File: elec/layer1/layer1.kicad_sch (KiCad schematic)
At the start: 114 parts, among them U1 DEV-15583, U2 CD74HC4067SM, U3 CD74HC4067SM

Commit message: fix: layer1 pcb
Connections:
- net +3V3: no longer U1.3.3V_1, U1.3.3V_2
- no-connect marks 25 -> 28
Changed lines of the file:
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@@
 	)
 	(no_connect
+		(at 154.94 109.22)
+	)
+	(no_connect
 		(at 196.85 203.2)
 	)
@@
 	)
 	(no_connect
+		(at 232.41 193.04)
+	)
+	(no_connect
 		(at 102.87 217.17)
 	)
@@
 	)
 	(no_connect
+		(at 196.85 228.6)
+	)
+	(no_connect
 		(at 196.85 205.74)
 	)
@@
 	)
 	(symbol
-		(lib_id "power:+3V3")
-		(at 196.85 228.6 90)
-		(unit 1)
-		(exclude_from_sim no)
-		(in_bom yes)
-		(on_board yes)
-		(dnp no)
-		(fields_autoplaced yes)
-		(property "Reference" "#PWR049"
-			(at 200.66 228.6 0)
-			(effects
-				(font
-					(size 1.27 1.27)
-				)
-				(hide yes)
-			)
-		)
-		(property "Value" "+3V3"
-			(at 193.04 228.5999 90)
-			(effects
-				(font
-					(size 1.27 1.27)
-				)
-				(justify left)
-			)
-		)
-		(property "Footprint" ""
-			(at 196.85 228.6 0)
-			(effects
-				(font
-					(size 1.27 1.27)
-				)
-				(hide yes)
-			)
-		)
-		(property "Datasheet" ""
-			(at 196.85 228.6 0)
-			(effects
-				(font
-					(size 1.27 1.27)
-				)
-				(hide yes)
-			)
-		)
-		(property "Description" "Power symbol creates a global label with name \"+3V3\""
-			(at 196.85 228.6 0)
-			(effects
-				(font
-					(size 1.27 1.27)
-				)
-				(hide yes)
-			)
-		)
-		(pin "1"
-		)
-		(instances
-			(project ""
-				(path "/68b2dc84-e8ac-4ad5-a4b5-71d0b0deb0c0"
-					(reference "#PWR049")
-					(unit 1)
-				)
-			)
-		)
-	)
-	(symbol
 		(lib_id "power:GND")
 		(at 114.3 222.25 90)
@@
 					(unit 1)
 				)
-			)
-		)
-	)
-	(symbol
-		(lib_id "power:+3V3")
-		(at 232.41 193.04 270)
-		(unit 1)
-		(exclude_from_sim no)
-		(in_bom yes)
-		(on_board yes)
-		(dnp no)
-		(fields_autoplaced yes)
-		(property "Reference" "#PWR050"
-			(at 228.6 193.04 0)
-			(effects
-				(font
-					(size 1.27 1.27)
-				)
-				(hide yes)
-			)
-		)
-		(property "Value" "+3V3"
-			(at 236.22 193.0399 90)
-			(effects
-				(font
-					(size 1.27 1.27)
-				)
-				(justify left)
-			)
-		)
-		(property "Footprint" ""
-			(at 232.41 193.04 0)
-			(effects
-				(font
-					(size 1.27 1.27)
-				)
-				(hide yes)
-			)
-		)
-		(property "Datasheet" ""
-			(at 232.41 193.04 0)
-			(effects
-				(font
-					(size 1.27 1.27)
-				)
-				(hide yes)
-			)
-		)
-		(property "Description" "Power symbol creates a global label with name \"+3V3\""
-			(at 232.41 193.04 0)
-			(effects
-				(font
-					(size 1.27 1.27)
-				)
-				(hide yes)
-			)
-		)
-		(pin "1"
-		)
-		(instances
-			(project ""
-				(path "/68b2dc84-e8ac-4ad5-a4b5-71d0b0deb0c0"
-					(reference "#PWR050")
-					(unit 1)
-				)

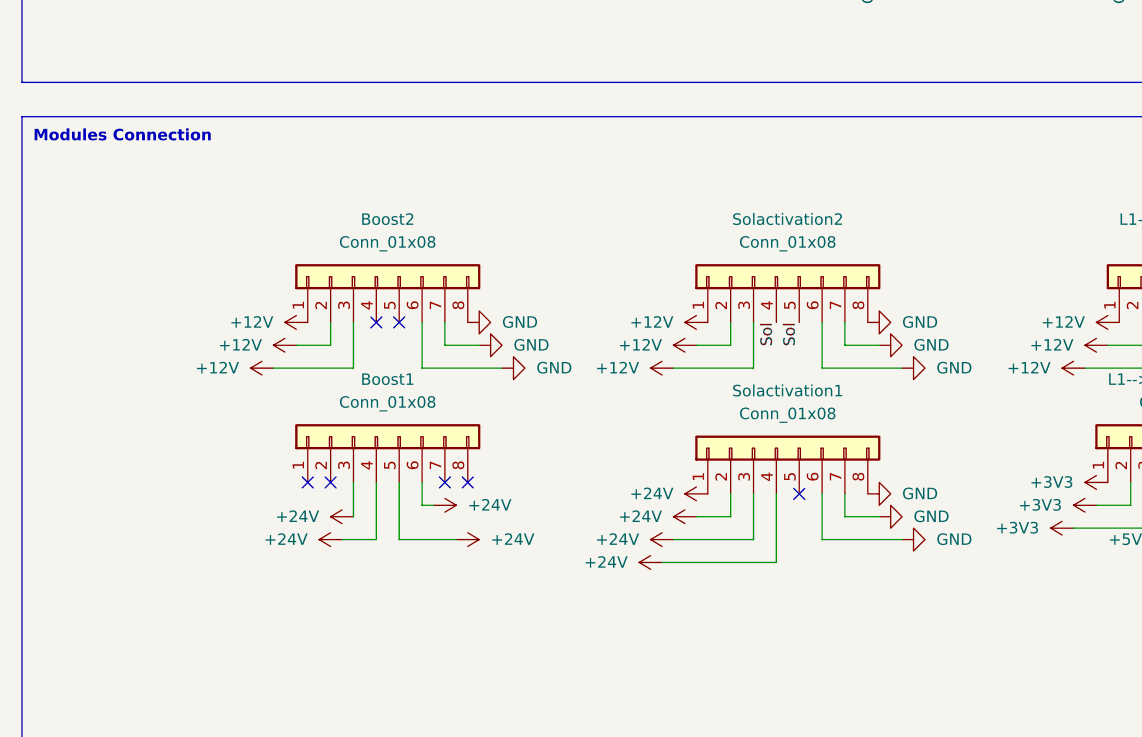
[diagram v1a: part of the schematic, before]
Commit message: l1: added some stuff havent connected data to drivers yet
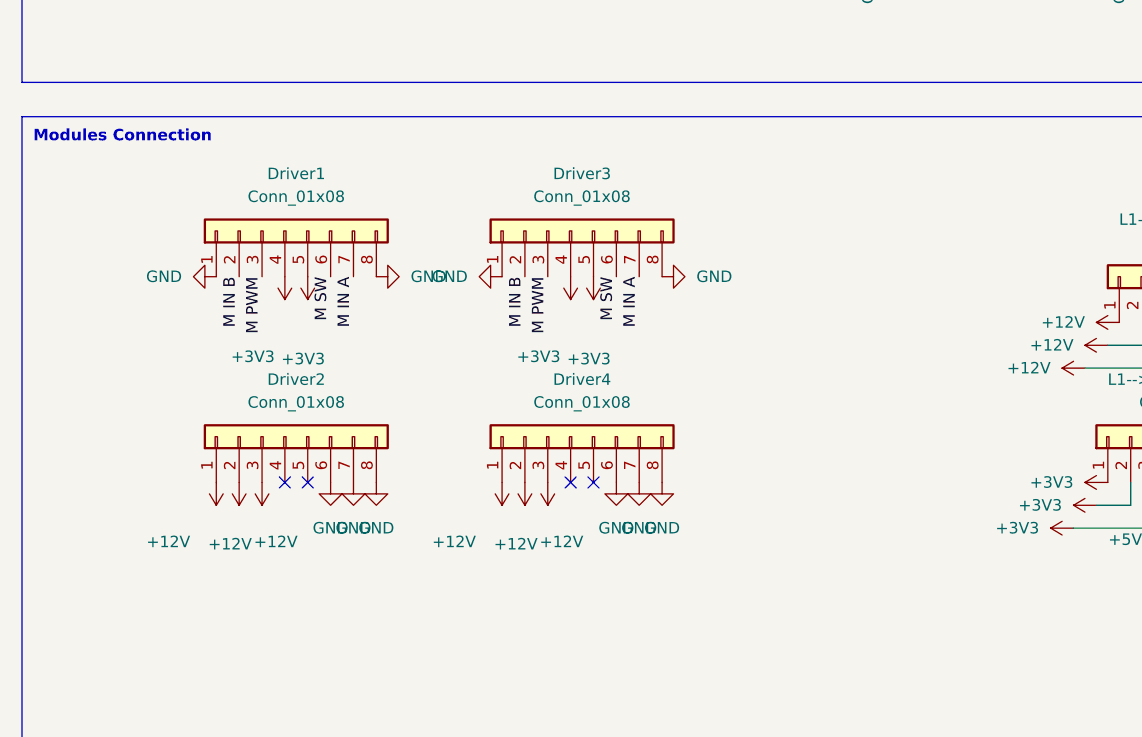
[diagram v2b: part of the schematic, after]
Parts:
- removed Boost1, Boost2, Solactivation1, Solactivation2: Conn_01x08, L1:PinHeader_1x08_P2.54mm_Vertical, symbol Connector_Generic:Conn_01x08
- added Driver1, Driver2, Driver3, Driver4: Conn_01x08, Pinheaders:PinHeader_1x08_P2.54mm_Vertical, symbol Connector_Generic:Conn_01x08
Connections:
- net +12V: now also Driver2.1 (Pin_1), Driver2.2 (Pin_2), Driver2.3 (Pin_3), Driver4.1 (Pin_1), Driver4.2 (Pin_2), Driver4.3 (Pin_3)
- net +3V3: now also Driver1.4 (Pin_4), Driver1.5 (Pin_5), Driver3.4 (Pin_4), Driver3.5 (Pin_5)
- net GND: now also Driver1.1 (Pin_1), Driver1.8 (Pin_8), Driver2.6 (Pin_6), Driver2.7 (Pin_7), Driver2.8 (Pin_8), Driver3.1 (Pin_1), Driver3.8 (Pin_8), Driver4.6 (Pin_6), Driver4.7 (Pin_7), Driver4.8 (Pin_8)
- new net M IN A: Driver1.7 (Pin_7), Driver3.7 (Pin_7)
- new net M IN B: Driver1.2 (Pin_2), Driver3.2 (Pin_2)
- new net M PWM: Driver1.3 (Pin_3), Driver3.3 (Pin_3)
- new net M SW: Driver1.6 (Pin_6), Driver3.6 (Pin_6)
- no-connect marks 28 -> 25

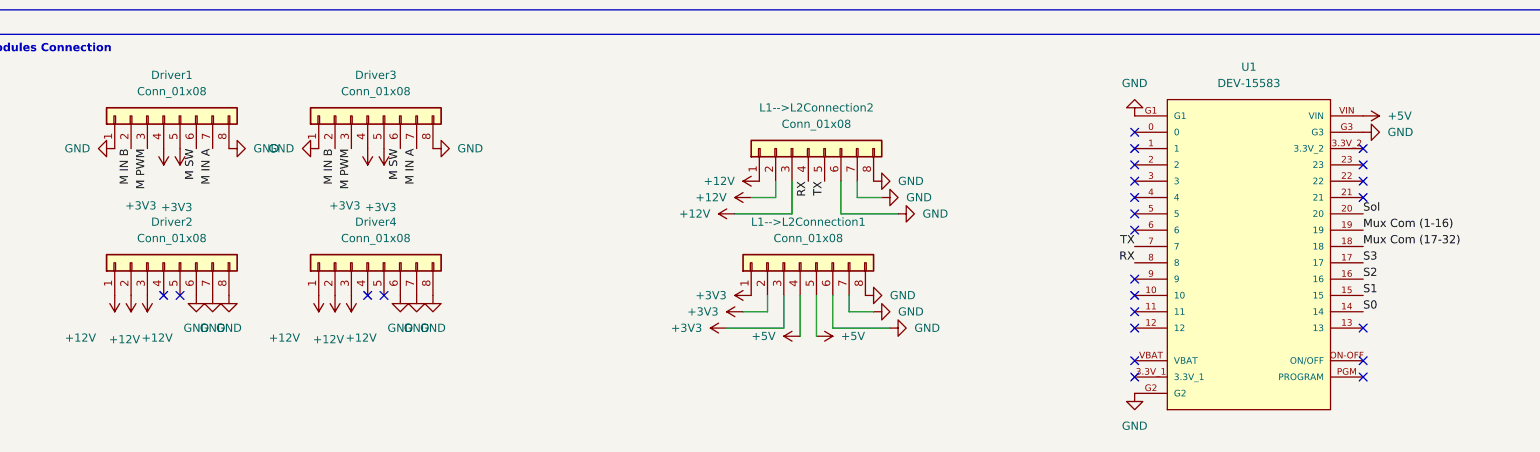
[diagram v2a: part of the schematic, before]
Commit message: connectred the pins for driver
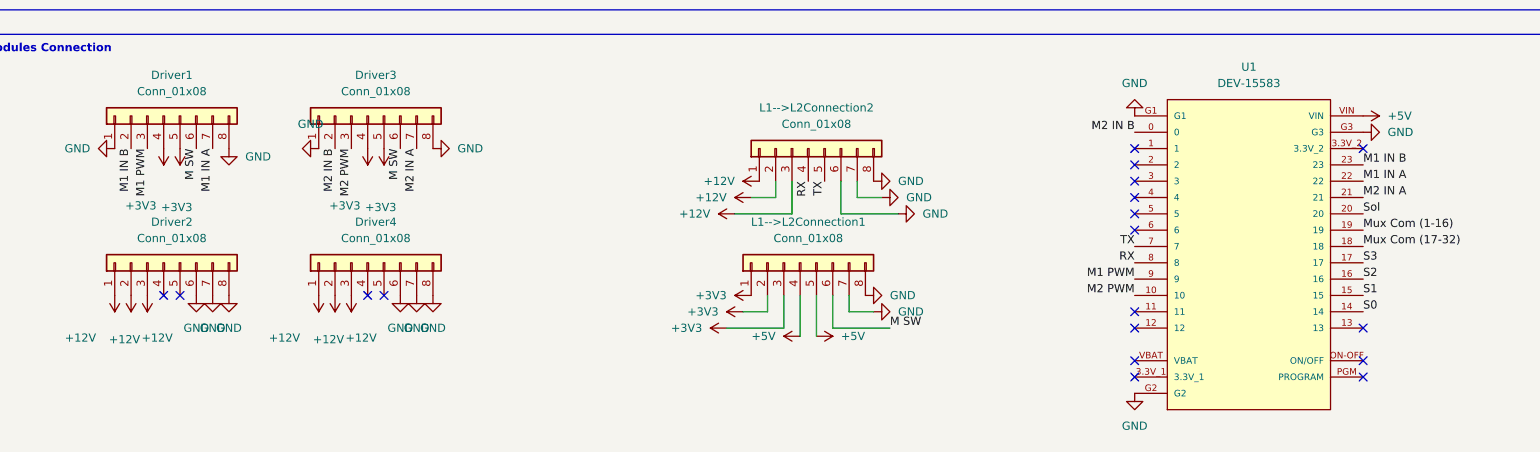
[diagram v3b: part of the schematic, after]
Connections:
- net GND: no longer L1-->L2Connection1.6 (Pin_6)
- net M SW: now also L1-->L2Connection1.6 (Pin_6)
- net M2 IN B: now reaches U1.0
- net M2 IN B: now also Driver3.2 (Pin_2)
- net M2 PWM: now reaches U1.10
- net M2 PWM: now also Driver3.3 (Pin_3)
- net M2 IN A: now reaches U1.21
- net M2 IN A: now also Driver3.7 (Pin_7)
- net M1 IN A: now reaches U1.22
- net M1 IN A: now also Driver1.7 (Pin_7)
- net M1 IN B: now reaches U1.23
- net M1 IN B: now also Driver1.2 (Pin_2)
- net M1 PWM: now reaches U1.9
- net M1 PWM: now also Driver1.3 (Pin_3)
- removed net M IN A: Driver1.7 (Pin_7), Driver3.7 (Pin_7)
- removed net M IN B: Driver1.2 (Pin_2), Driver3.2 (Pin_2)
- removed net M PWM: Driver1.3 (Pin_3), Driver3.3 (Pin_3)
- no-connect marks 25 -> 19
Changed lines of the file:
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@@
 	)
 	(no_connect
-		(at 196.85 215.9)
-	)
-	(no_connect
-		(at 196.85 213.36)
-	)
-	(no_connect
 		(at 196.85 195.58)
 	)
@@
 	)
 	(no_connect
-		(at 232.41 200.66)
-	)
-	(no_connect
 		(at 232.41 226.06)
 	)
 	(no_connect
-		(at 196.85 190.5)
-	)
-	(no_connect
-		(at 232.41 198.12)
-	)
-	(no_connect
 		(at 154.94 109.22)
 	)
@@
 	)
 	(no_connect
-		(at 232.41 195.58)
-	)
-	(no_connect
 		(at 80.01 215.9)
 	)
@@
 		)
 	)
+	(label "M2 IN B"
+		(at 196.85 190.5 180)
+		(effects
+			(font
+				(size 1.27 1.27)
+			)
+			(justify right bottom)
+		)
+	)
 	(label "TX"
 		(at 196.85 208.28 180)
@@
 		)
 	)
+	(label "M1 PWM"
+		(at 196.85 213.36 180)
+		(effects
+			(font
+				(size 1.27 1.27)
+			)
+			(justify right bottom)
+		)
+	)
 	(label "TX"
 		(at 148.59 198.12 270)
@@
 		)
 	)
-	(label "M IN A"
+	(label "M2 IN A"
 		(at 85.09 193.04 270)
 		(effects
@@
 		)
 	)
-	(label "M IN A"
+	(label "M1 IN A"
 		(at 53.34 193.04 270)
 		(effects
@@
 		)
 	)
-	(label "M IN B"
+	(label "M1 IN B"
 		(at 40.64 193.04 270)
 		(effects
@@
 		)
 	)
+	(label "M2 PWM"
+		(at 196.85 215.9 180)
+		(effects
+			(font
+				(size 1.27 1.27)
+			)
+			(justify right bottom)
+		)
+	)
 	(label "S0"
 		(at 232.41 218.44 0)
@@
 		)
 	)
+	(label "M2 IN A"
+		(at 232.41 200.66 0)
+		(effects
+			(font
+				(size 1.27 1.27)
+			)
+			(justify left bottom)
+		)
+	)
 	(label "Sol"
 		(at 232.41 203.2 0)
@@
 		)
 	)
+	(label "M1 IN B"
+		(at 232.41 195.58 0)
+		(effects
+			(font
+				(size 1.27 1.27)
+			)
+			(justify left bottom)
+		)
+	)
 	(label "S2"
 		(at 125.73 147.32 180)
@@
 	)
 	(label "M SW"
+		(at 158.75 220.98 0)
+		(effects
+			(font
+				(size 1.27 1.27)
+			)
+			(justify left bottom)
+		)
+	)
+	(label "M1 IN A"
+		(at 232.41 198.12 0)
+		(effects
+			(font
+				(size 1.27 1.27)
+			)
+			(justify left bottom)
+		)
+	)
+	(label "M SW"
 		(at 50.8 193.04 270)
 		(effects
@@
 		)
 	)
-	(label "M IN B"
+	(label "M2 IN B"
 		(at 72.39 193.04 270)
 		(effects
@@
 		)
 	)
-	(label "M PWM"
+	(label "M2 PWM"
 		(at 74.93 193.04 270)
 		(effects
@@
 		)
 	)
-	(label "M PWM"
+	(label "M1 PWM"
 		(at 43.18 193.04 270)
 		(effects
@@
 	(symbol
 		(lib_id "power:GND")
-		(at 55.88 193.04 90)
+		(at 55.88 193.04 0)
 		(unit 1)
 		(exclude_from_sim no)
@@
 		(fields_autoplaced yes)
 		(property "Reference" "#PWR016"
-			(at 62.23 193.04 0)
+			(at 55.88 199.39 0)
 			(effects
 				(font
@@
 		)
 		(property "Value" "GND"
-			(at 59.69 193.0399 90)
+			(at 58.42 194.3099 0)
 			(effects
 				(font
 					(size 1.27 1.27)
 				)
-				(justify right)
+				(justify left)
 			)
 		)
@@
 		(on_board yes)
 		(dnp no)
-		(property "Reference" "#PWR012"
+		(property "Reference" "#PWR0103"
 			(at 43.18 212.09 0)
 			(effects
@@
 			(project "layer1"
 				(path "/68b2dc84-e8ac-4ad5-a4b5-71d0b0deb0c0"
-					(reference "#PWR012")
+					(reference "#PWR0103")
 					(unit 1)
 				)
@@
 		)
 		(property "Value" "GND"
-			(at 66.04 193.0399 90)
+			(at 68.58 189.23 90)
 			(effects
 				(font
 					(size 1.27 1.27)
 				)
-				(justify right)
 			)
 		)
@@
 	)
 	(symbol
-		(lib_id "power:GND")
-		(at 158.75 220.98 90)
-		(unit 1)
-		(exclude_from_sim no)
-		(in_bom yes)
-		(on_board yes)
-		(dnp no)
-		(fields_autoplaced yes)
-		(property "Reference" "#PWR056"
-			(at 165.1 220.98 0)
-			(effects
-				(font
-					(size 1.27 1.27)
-				)
-				(hide yes)
-			)
-		)
-		(property "Value" "GND"
-			(at 162.56 220.9799 90)
-			(effects
-				(font
-					(size 1.27 1.27)
-				)
-				(justify right)
-			)
-		)
-		(property "Footprint" ""
-			(at 158.75 220.98 0)
-			(effects
-				(font
-					(size 1.27 1.27)
-				)
-				(hide yes)
-			)
-		)
-		(property "Datasheet" ""
-			(at 158.75 220.98 0)
-			(effects
-				(font
-					(size 1.27 1.27)
-				)
-				(hide yes)
-			)
-		)
-		(property "Description" "Power symbol creates a global label with name \"GND\" , ground"
-			(at 158.75 220.98 0)
-			(effects
-				(font
-					(size 1.27 1.27)
-				)
-				(hide yes)
-			)
-		)
-		(pin "1"
-		)
-		(instances
-			(project "layer1"
-				(path "/68b2dc84-e8ac-4ad5-a4b5-71d0b0deb0c0"
-					(reference "#PWR056")
-					(unit 1)
-				)
-			)
-		)
-	)
-	(symbol
 		(lib_id "Device:LED")
 		(at 101.6 58.42 90)
@@
 		(on_board yes)
 		(dnp no)
-		(property "Reference" "#PWR014"
+		(property "Reference" "#PWR0102"
 			(at 45.72 189.23 0)
 			(effects
@@
 			(project "layer1"
 				(path "/68b2dc84-e8ac-4ad5-a4b5-71d0b0deb0c0"
-					(reference "#PWR014")
+					(reference "#PWR0102")
 					(unit 1)
 				)

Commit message: l2 domne
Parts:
- removed L1-->L2Connection1, L1-->L2Connection2: Conn_01x08, L1:PinHeader_1x08_P2.54mm_Vertical, symbol Connector_Generic:Conn_01x08
- added Driver5, Driver6, Driver7, Driver8: Conn_01x08, Connector_JST:JST_XH_B8B-XH-A_1x08_P2.50mm_Vertical, symbol Connector_Generic:Conn_01x08
- added L1-->l2Connection1: Conn_01x09, Pinheaders:PinHeader_1x09_P2.54mm_Vertical, symbol Connector_Generic:Conn_01x09
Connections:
- net +12V: now also Driver6.1 (Pin_1), Driver6.2 (Pin_2), Driver6.3 (Pin_3), Driver8.1 (Pin_1), Driver8.2 (Pin_2), Driver8.3 (Pin_3)
- net +3V3: now also Driver5.4 (Pin_4), Driver5.5 (Pin_5), Driver7.4 (Pin_4), Driver7.5 (Pin_5)
- net +5V: now also L1-->l2Connection1.6 (Pin_6), L1-->l2Connection1.7 (Pin_7)
- net GND: now also Driver5.1 (Pin_1), Driver5.8 (Pin_8), Driver6.6 (Pin_6), Driver6.7 (Pin_7), Driver6.8 (Pin_8), Driver7.1 (Pin_1), Driver7.8 (Pin_8), Driver8.6 (Pin_6), Driver8.7 (Pin_7), Driver8.8 (Pin_8), L1-->l2Connection1.8 (Pin_8), L1-->l2Connection1.9 (Pin_9)
- net M SW: now also Driver7.6 (Pin_6), L1-->l2Connection1.3 (Pin_3)
- net M2 IN A: now also Driver7.7 (Pin_7)
- net M2 PWM: now also Driver7.3 (Pin_3)
- net RX: now also L1-->l2Connection1.5 (Pin_5)
- net TX: now also L1-->l2Connection1.4 (Pin_4)
- net Dribbler Data: now reaches U1.1
- net Dribbler Data: now also L1-->l2Connection1.1 (Pin_1)
- net M3 PWM: now reaches U1.11
- net M3 PWM: now also Driver5.3 (Pin_3)
- net M4 PWM: now reaches U1.12
- net LightGateLDR: now reaches U1.2
- net LightGateLDR: now also L1-->l2Connection1.2 (Pin_2)
- net M3 IN A: now reaches U1.3
- net M3 IN A: now also Driver5.7 (Pin_7)
- net M3 IN B: now reaches U1.4
- net M3 IN B: now also Driver5.2 (Pin_2)
- net M4 IN A: now reaches U1.5
- net M4 IN B: now reaches U1.6
- net M4 IN B: now also Driver7.2 (Pin_2)
- new net M SW3: Driver5.6 (Pin_6)
- no-connect marks 19 -> 15
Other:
- moved on the sheet: Driver1, Driver2, Driver3, Driver4

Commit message: l1 half motors done
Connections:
- net M SW3 is gone; now on net M SW: Driver5.6 (Pin_6)
- net +5V: now also L1-->l2Connection1.8 (Pin_8); no longer L1-->l2Connection1.6 (Pin_6)
- net Dribbler Data: now also L1-->l2Connection1.2 (Pin_2), U1.0; no longer L1-->l2Connection1.1 (Pin_1), U1.1
- net GND: no longer L1-->l2Connection1.8 (Pin_8)
- net LightGateLDR: now also L1-->l2Connection1.1 (Pin_1), U1.1; no longer L1-->l2Connection1.2 (Pin_2), U1.2
- net M1 PWM: now also U1.10; no longer U1.9
- net M2 IN A: no longer Driver7.7 (Pin_7)
- net M2 IN B: now also U1.4; no longer U1.0
- net M2 PWM: now also U1.11; no longer Driver7.3 (Pin_3), U1.10
- net M3 IN A: now also U1.5; no longer U1.3
- net M3 IN B: now also U1.6; no longer U1.4
- net M3 PWM: now also U1.12; no longer U1.11
- net M4 IN A: now also Driver7.7 (Pin_7), U1.2; no longer U1.5
- net M4 IN B: now also U1.3; no longer U1.6
- net M4 PWM: now also Driver7.3 (Pin_3), U1.9; no longer U1.12
- net RX: now also L1-->l2Connection1.4 (Pin_4); no longer L1-->l2Connection1.5 (Pin_5)
- net Sol: now also L1-->l2Connection1.6 (Pin_6)
- net TX: now also L1-->l2Connection1.5 (Pin_5); no longer L1-->l2Connection1.4 (Pin_4)
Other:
- moved on the sheet: L1-->l2Connection1

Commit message: er
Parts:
- L1-->l2Connection1: footprint Pinheaders:PinHeader_1x09_P2.54mm_Vertical -> Connector_JST:JST_XH_B9B-XH-A_1x09_P2.50mm_Vertical
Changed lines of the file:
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@@
 			)
 		)
-		(property "Footprint" "Pinheaders:PinHeader_1x09_P2.54mm_Vertical"
+		(property "Footprint" "Connector_JST:JST_XH_B9B-XH-A_1x09_P2.50mm_Vertical"
 			(at 63.5 218.44 0)
 			(effects
